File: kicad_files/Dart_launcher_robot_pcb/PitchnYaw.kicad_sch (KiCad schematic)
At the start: 4 parts, among them J12 Conn_01x04_Pin, J16 Conn_01x03_Pin, J3 Conn_01x05_Pin, J4 Conn_01x03_Pin

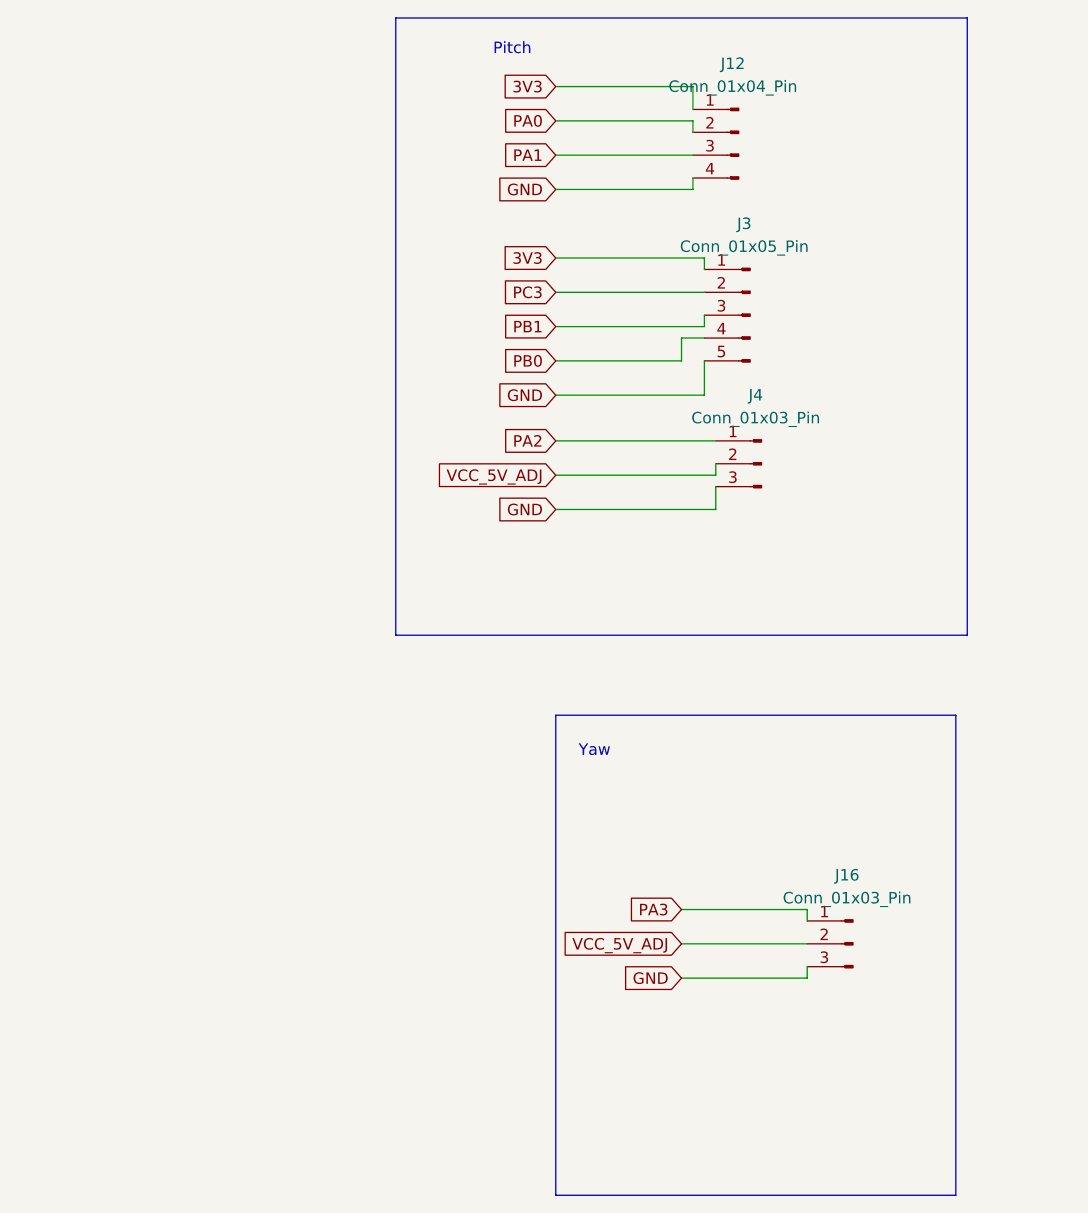
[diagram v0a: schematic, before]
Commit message: pcb design and changes to the pitch_yaw_launcher_code
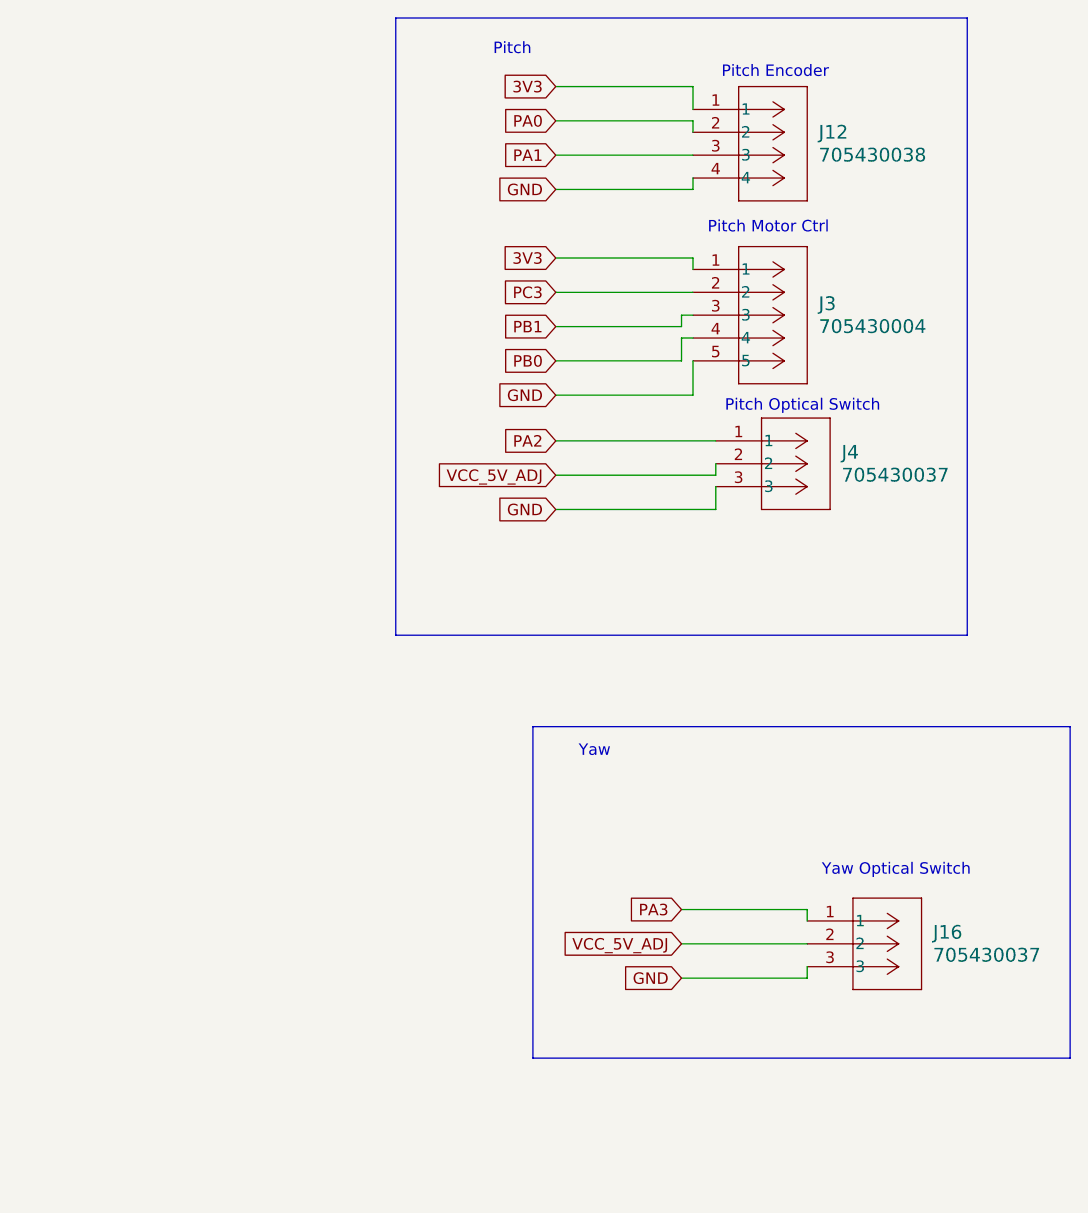
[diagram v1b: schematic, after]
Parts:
- removed J12: Conn_01x04_Pin, Connector_PinHeader_2.54mm:PinHeader_1x04_P2.54mm_Vertical, symbol Connector:Conn_01x04_Pin
- removed J16, J4: Conn_01x03_Pin, Connector_PinHeader_2.54mm:PinHeader_1x03_P2.54mm_Vertical, symbol Connector:Conn_01x03_Pin
- removed J3: Conn_01x05_Pin, Connector_PinHeader_2.54mm:PinHeader_1x05_P2.54mm_Vertical, symbol Connector:Conn_01x05_Pin
- added J12: 705430038, CONN_SDA-70543-xxxx_04_MOL, symbol Molex_705430038:705430038
- added J16, J4: 705430037, CONN_SDA-70543-xxxx_03_MOL, symbol Molex_0705430037:705430037
- added J3: 705430004, footprints:CONN_SDA-70543-xxxx_05_MOL, symbol Molex_070543:705430004
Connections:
- net 3V3: now also J12.1, J3.1
- net GND: now also J12.4, J16.3, J3.5, J4.3
- net PA0: now also J12.2
- net PA1: now also J12.3
- net PA2: now also J4.1
- net PA3: now also J16.1
- net PB0: now also J3.4
- net PB1: now also J3.3
- net PC3: now also J3.2
- net VCC_5V_ADJ: now also J16.2, J4.2
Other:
- note added: "Pitch Encoder"
- note added: "Pitch Motor Ctrl"
- note added: "Pitch Optical Switch"
- note added: "Yaw Optical Switch"

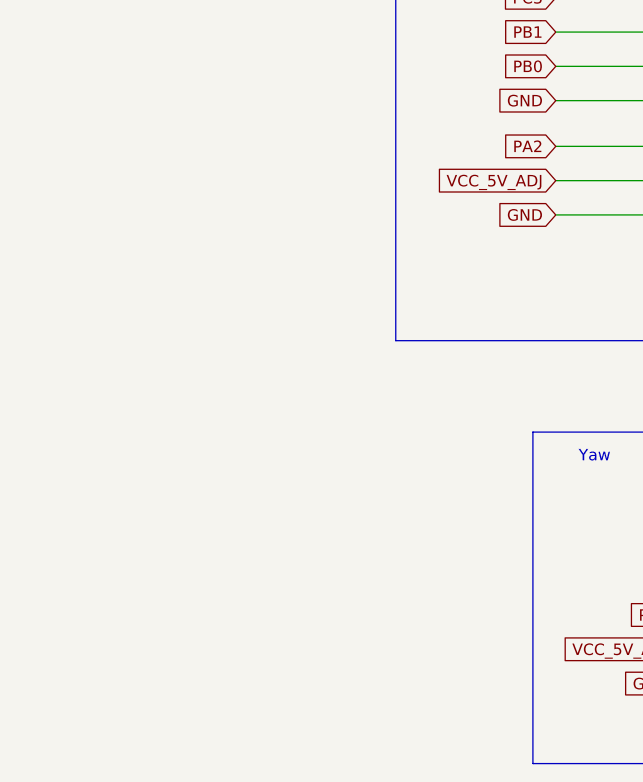
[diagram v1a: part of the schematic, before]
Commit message: the launcher task canabalise the  feeder task
update the frequency of the communication  to handle longer cable length

update the pitch yaw to handle  control of all the different type of control method

update screen to have an auto tab and a rc tab
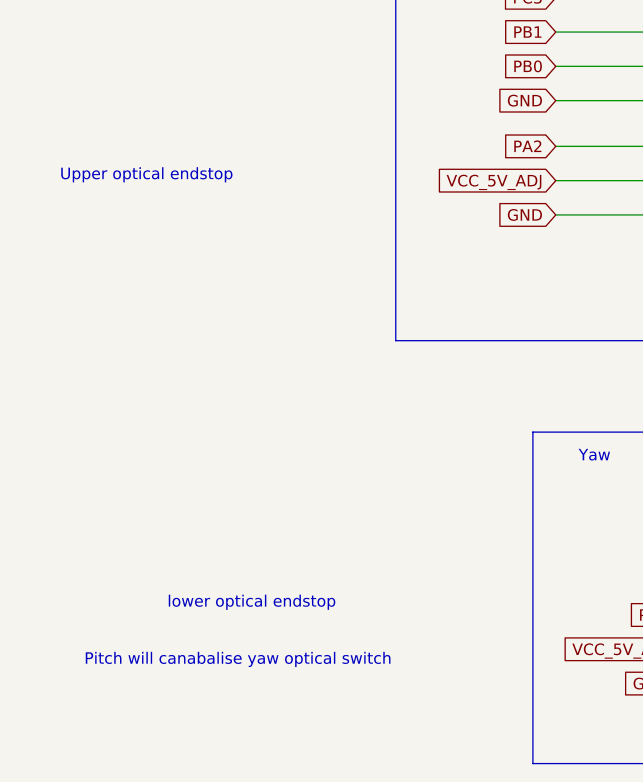
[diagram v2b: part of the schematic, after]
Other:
- note added: "Pitch will canabalise yaw optical switch"
- note added: "Upper optical endstop"
- note added: "lower optical endstop"
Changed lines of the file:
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@@
+		)
+	)
+	(text "lower optical endstop"
+		(exclude_from_sim no)
+		(at 79.248 120.65 0)
+		(effects
+			(font
+				(size 1.27 1.27)
+			)
 		)
 	)
@@
 		)
 	)
+	(text "Upper optical endstop"
+		(exclude_from_sim no)
+		(at 67.564 73.152 0)
+		(effects
+			(font
+				(size 1.27 1.27)
+			)
+		)
+	)
 	(text "Yaw Optical Switch"
 		(exclude_from_sim no)
@@
 		(effects
 			(font
+				(size 1.27 1.27)
+			)
+		)
+	)
+	(text "Pitch will canabalise yaw optical switch\n"
+		(exclude_from_sim no)
+		(at 77.724 127 0)
+		(effects
+			(font
